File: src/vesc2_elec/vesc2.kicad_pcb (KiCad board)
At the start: 6 copper layers, 0 parts

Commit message: Most the layout done im playing cs2
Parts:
- added C101: 2u2, Capacitor_SMD:C_0603_1608Metric, F.Cu at (150.4, 106.1)
- added C102: 2u2, Capacitor_SMD:C_0603_1608Metric, F.Cu at (150.4, 108.7)
- added C103: 220n, Capacitor_SMD:C_0402_1005Metric, B.Cu at (191.0, 115.5)
- added C104: 220n, Capacitor_SMD:C_0402_1005Metric, B.Cu at (195.5, 116.5)
- added C105: 220n, Capacitor_SMD:C_0402_1005Metric, B.Cu at (198.0, 126.2)
- added C106: 220n, Capacitor_SMD:C_0402_1005Metric, B.Cu at (186.8, 130.5)
- added C107: 220n, Capacitor_SMD:C_0402_1005Metric, B.Cu at (183.0, 119.5)
- added C108: 10p, Capacitor_SMD:C_0402_1005Metric, B.Cu at (181.8, 127.5)
- added C109: 10p, Capacitor_SMD:C_0402_1005Metric, B.Cu at (179.2, 125.2)
- added C110: 4u7, Capacitor_SMD:C_0805_2012Metric, B.Cu at (197.2, 116.8)
- added C111: 10n, Capacitor_SMD:C_0402_1005Metric, F.Cu at (152.0, 115.8)
- added C112: 100n, Capacitor_SMD:C_0402_1005Metric, F.Cu at (152.0, 117.8)
- added C113: 220n, Capacitor_SMD:C_0402_1005Metric, F.Cu at (152.0, 119.8)
- added C114: 33n, Capacitor_SMD:C_0402_1005Metric, B.Cu at (182.3, 121.8)
- added C115: 220n, Capacitor_SMD:C_0402_1005Metric, F.Cu at (152.0, 123.7)
- added C116: 220n, Capacitor_SMD:C_0402_1005Metric, F.Cu at (154.8, 113.9)
- added C117: 220n, Capacitor_SMD:C_0402_1005Metric, F.Cu at (154.8, 115.8)
- added C118: 220n, Capacitor_SMD:C_0402_1005Metric, F.Cu at (154.8, 117.8)
- added C119: 2u2, Capacitor_SMD:C_0603_1608Metric, B.Cu at (194.2, 113.2)
- added C120: 2u2, Capacitor_SMD:C_0603_1608Metric, B.Cu at (192.5, 113.2)
- added C121: 10u, Capacitor_SMD:C_1206_3216Metric, B.Cu at (175.8, 117.8)
- added C122: 2u2, Capacitor_SMD:C_0603_1608Metric, B.Cu at (179.0, 121.0)
- added C123: 10u, Capacitor_SMD:C_1206_3216Metric, B.Cu at (172.0, 120.5)
- added C124: 270u, Capacitor_SMD:CP_Elec_10x10, F.Cu at (193.0, 92.8)
- added C125: 270u, Capacitor_SMD:CP_Elec_10x10, F.Cu at (172.2, 92.5)
- added C201: 1n, Capacitor_SMD:C_0402_1005Metric, B.Cu at (175.0, 115.3)
- added C202: 4u7, Capacitor_SMD:C_1206_3216Metric, B.Cu at (183.8, 113.8)
- added C203: 1n, Capacitor_SMD:C_0402_1005Metric, B.Cu at (172.5, 115.3)
- added C204: 10n, Capacitor_SMD:C_0402_1005Metric, B.Cu at (189.8, 113.1)
- added C205: 2u2, Capacitor_SMD:C_0603_1608Metric, B.Cu at (176.0, 113.3)
- added C206: 2u2, Capacitor_SMD:C_0603_1608Metric, B.Cu at (172.5, 113.3)
- added C207: 100p, Capacitor_SMD:C_0402_1005Metric, B.Cu at (187.8, 114.1)
- added C208: 33n, Capacitor_SMD:C_0603_1608Metric, B.Cu at (179.5, 113.3)
- added C209: 4u7, Capacitor_SMD:C_1210_3225Metric, B.Cu at (171.0, 104.8)
- added C210: 10n, Capacitor_SMD:C_0402_1005Metric, B.Cu at (189.3, 103.3)
- added C211: 100n, Capacitor_SMD:C_0603_1608Metric, B.Cu at (189.3, 100.8)
- added C212: 330n, Capacitor_SMD:C_0603_1608Metric, B.Cu at (183.5, 101.3)
- added C213: 330n, Capacitor_SMD:C_0603_1608Metric, B.Cu at (180.3, 101.3)
- added C214: 330n, Capacitor_SMD:C_0603_1608Metric, B.Cu at (177.0, 101.3)
- added C215: 1n, Capacitor_SMD:C_0402_1005Metric, B.Cu at (174.8, 101.0)
- added C216: 1n, Capacitor_SMD:C_0402_1005Metric, B.Cu at (173.5, 101.0)
- added C217: 4u7, Capacitor_SMD:C_1210_3225Metric, B.Cu at (189.8, 106.8)
- added C218: 22u, Capacitor_SMD:C_1210_3225Metric, B.Cu at (184.0, 97.8)
- added C301: 1n, Capacitor_SMD:C_0402_1005Metric, B.Cu at (194.1, 91.4)
- added C302: 1n, Capacitor_SMD:C_0402_1005Metric, B.Cu at (187.7, 91.5)
- added C303: 3n3, Capacitor_SMD:C_0402_1005Metric, B.Cu at (196.4, 92.0)
- added C401: 1n, Capacitor_SMD:C_0402_1005Metric, B.Cu at (182.4, 91.4)
- added C402: 1n, Capacitor_SMD:C_0402_1005Metric, B.Cu at (176.1, 91.5)
- added C403: 3n3, Capacitor_SMD:C_0402_1005Metric, B.Cu at (184.8, 92.0)
- added C501: 1n, Capacitor_SMD:C_0402_1005Metric, B.Cu at (171.1, 91.4)
- added C502: 1n, Capacitor_SMD:C_0402_1005Metric, B.Cu at (164.7, 91.5)
- added C503: 3n3, Capacitor_SMD:C_0402_1005Metric, B.Cu at (173.4, 92.0)
- added D101: 30V, Diode_SMD:D_SMF, B.Cu at (191.2, 82.5)
- added D102: DTVS, Package_TO_SOT_SMD:SOT-523, F.Cu at (154.7, 129.6)
- added D103: 3V3, Package_DFN_QFN:Diodes_UDFN-10_1.0x2.5mm_P0.5mm, F.Cu at (141.4, 115.0)
- added D104: 3V3, Package_DFN_QFN:Diodes_UDFN-10_1.0x2.5mm_P0.5mm, F.Cu at (144.6, 115.0)
- added D105: WS2812B-2020, Bluesat:WS2812B-2020, F.Cu at (183.0, 130.0)
- added D106: WS2812B-2020, Bluesat:WS2812B-2020, F.Cu at (179.4, 130.0)
- added D107: WS2812B-2020, Bluesat:WS2812B-2020, F.Cu at (175.9, 130.0)
- added D201: D_Schottky, Diode_SMD:D_SOD-123, B.Cu at (187.0, 99.8)
- added J101: XT-30-TOP, Bluesat:XT30PW-M_1x02_P2.50mm_Top_mount, F.Cu at (191.0, 78.5)
- added J102: HALL/ENCODER, Bluesat:SM06B-PASS, F.Cu at (163.0, 108.0)
- added J103: SM02B-PASS, Bluesat:BM02B-PASS, F.Cu at (169.0, 122.0)
- added J104: IDC6, Bluesat:IDC6, F.Cu at (195.0, 106.0)
- added J105: MR_60_TOP, Bluesat:MR60-F-TopMount, F.Cu at (173.0, 80.0)
- added L101: 600R, Resistor_SMD:R_0402_1005Metric, B.Cu at (193.2, 115.5)
- added L201: 47u, Inductor_SMD:L_Changjiang_FXL0630, F.Cu at (184.0, 99.8)
- added Q301: IRFH7440TRPBF, Bluesat:PQFN_5x6mm_E_DGS, B.Cu at (195.2, 87.3)
- added Q302: IRFH7440TRPBF, Bluesat:PQFN_5x6mm_E_DGS, B.Cu at (189.7, 87.3)
- added Q401: IRFH7440TRPBF, Bluesat:PQFN_5x6mm_E_DGS, B.Cu at (183.7, 87.3)
- added Q402: IRFH7440TRPBF, Bluesat:PQFN_5x6mm_E_DGS, B.Cu at (178.1, 87.3)
- added Q501: IRFH7440TRPBF, Bluesat:PQFN_5x6mm_E_DGS, B.Cu at (172.2, 87.3)
- added Q502: IRFH7440TRPBF, Bluesat:PQFN_5x6mm_E_DGS, B.Cu at (166.7, 87.3)
- added R101: 10k, Resistor_SMD:R_0402_1005Metric, F.Cu at (141.1, 107.9)
- added R102: 100k, Resistor_SMD:R_0402_1005Metric, F.Cu at (141.1, 109.9)
- added R103: 2k2, Resistor_SMD:R_0402_1005Metric, F.Cu at (141.1, 111.9)
- added R104: 2k2, Resistor_SMD:R_0402_1005Metric, F.Cu at (144.0, 105.9)
- added R105: 2k2, Resistor_SMD:R_0402_1005Metric, F.Cu at (144.0, 107.9)
- added R106: 10k, Resistor_SMD:R_0402_1005Metric, F.Cu at (144.0, 109.9)
- added R107: 220k, Resistor_SMD:R_0402_1005Metric, B.Cu at (181.2, 119.2)
- added R108: 100k, Resistor_SMD:R_0402_1005Metric, F.Cu at (146.9, 105.9)
- added R109: 10k, Resistor_SMD:R_0402_1005Metric, B.Cu at (181.2, 120.5)
- added R110: 470R, Resistor_SMD:R_0402_1005Metric, B.Cu at (182.2, 123.0)
- added R201: 15k, Resistor_SMD:R_0402_1005Metric, B.Cu at (187.8, 115.3)
- added R202: 4k7, Resistor_SMD:R_0402_1005Metric, B.Cu at (189.3, 110.1)
- added R203: 220k, Resistor_SMD:R_0402_1005Metric, B.Cu at (187.8, 112.8)
- added R204: 1k, Resistor_SMD:R_0402_1005Metric, B.Cu at (180.5, 115.6)
- added R205: 2k2, Resistor_SMD:R_0402_1005Metric, B.Cu at (179.0, 115.6)
- added R206: 1k, Resistor_SMD:R_0402_1005Metric, B.Cu at (176.3, 115.3)
- added R207: 1k, Resistor_SMD:R_0402_1005Metric, B.Cu at (173.8, 115.3)
- added R208: 10k, Resistor_SMD:R_0402_1005Metric, B.Cu at (185.0, 116.1)
- added R209: 10k, Resistor_SMD:R_0402_1005Metric, B.Cu at (182.5, 116.1)
- added R210: 220k, Resistor_SMD:R_0402_1005Metric, B.Cu at (189.3, 111.3)
- added R301: 10R, Resistor_SMD:R_0402_1005Metric, B.Cu at (194.1, 93.8)
- added R302: 10R, Resistor_SMD:R_0402_1005Metric, B.Cu at (187.7, 94.0)
- added R303: 4k7, Resistor_SMD:R_0402_1005Metric, B.Cu at (194.1, 92.5)
- added R304: 4k7, Resistor_SMD:R_0402_1005Metric, B.Cu at (187.7, 92.8)
- added R305: 1m, Resistor_SMD:R_2512_6332Metric, B.Cu at (190.8, 94.8)
- added R306: 10R, Resistor_SMD:R_0402_1005Metric, B.Cu at (197.2, 94.2)
- added R307: 10R, Resistor_SMD:R_0402_1005Metric, B.Cu at (195.8, 94.2)
- added R401: 10R, Resistor_SMD:R_0402_1005Metric, B.Cu at (182.4, 93.8)
- added R402: 10R, Resistor_SMD:R_0402_1005Metric, B.Cu at (176.1, 94.0)
- added R403: 4k7, Resistor_SMD:R_0402_1005Metric, B.Cu at (182.4, 92.5)
- added R404: 4k7, Resistor_SMD:R_0402_1005Metric, B.Cu at (176.1, 92.8)
- added R405: 1m, Resistor_SMD:R_2512_6332Metric, B.Cu at (179.2, 94.8)
- added R406: 10R, Resistor_SMD:R_0402_1005Metric, B.Cu at (185.7, 94.2)
- added R407: 10R, Resistor_SMD:R_0402_1005Metric, B.Cu at (184.2, 94.2)
- added R501: 10R, Resistor_SMD:R_0402_1005Metric, B.Cu at (171.1, 93.8)
- added R502: 10R, Resistor_SMD:R_0402_1005Metric, B.Cu at (164.7, 94.0)
- added R503: 4k7, Resistor_SMD:R_0402_1005Metric, B.Cu at (171.1, 92.5)
- added R504: 4k7, Resistor_SMD:R_0402_1005Metric, B.Cu at (164.7, 92.8)
- added R505: 1m, Resistor_SMD:R_2512_6332Metric, B.Cu at (167.8, 94.8)
- added R506: 10R, Resistor_SMD:R_0402_1005Metric, B.Cu at (174.2, 94.2)
- added R507: 10R, Resistor_SMD:R_0402_1005Metric, B.Cu at (172.8, 94.2)
- added TH101: 10k, Resistor_SMD:R_0402_1005Metric, F.Cu at (146.9, 111.9)
- added U101: STM32G474_VESC, Bluesat:LQFP-64-0.5, B.Cu at (190.5, 123.0)
- added U102: TCAN1462V, Package_SO:SOIC-8_3.9x4.9mm_P1.27mm, B.Cu at (174.5, 125.8)
- added U103: HX4002, Package_TO_SOT_SMD:SOT-23-6, B.Cu at (175.8, 121.0)
- added U201: DRV8301, Bluesat:HTSSOP-56_6.1x14-0.5-EP, B.Cu at (180.5, 107.3)
- added Y101: 24Mhz, Crystal:Crystal_SMD_2016-4Pin_2.0x1.6mm, B.Cu at (181.8, 125.2)
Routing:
- net GND: vias 0 -> 15
- added copper zone on In2.Cu, net GND
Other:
- board outline added: 36 x 57 mm

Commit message: finished routing :)
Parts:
- C101, C102, C111, C112, C113, C115, C116, C117, C118, D102, D103, D104, R101, R102, R103, R104, R105, R106, R108, TH101: moved to B.Cu
- J102: footprint Bluesat:SM06B-PASS -> Bluesat:BM06B-PASS
- moved D103 55.4 mm to (196.8, 113.2), turned to 90 degrees
- moved R102 55.2 mm to (196.2, 107.0)
- moved TH101 54.8 mm to (193.8, 83.4), turned to 180 degrees
- moved R108 46.6 mm to (193.5, 107.0)
- moved R101 40.3 mm to (180.2, 117.5), turned to 180 degrees
- moved C111 39.4 mm to (191.0, 110.5), turned to -90 degrees
- moved C101 34.7 mm to (183.2, 117.2)
- moved C116 34.2 mm to (185.0, 130.0), turned to 180 degrees
- moved C113 31.3 mm to (181.5, 130.0), turned to 180 degrees
- moved R103 27.7 mm to (168.2, 117.2), turned to 180 degrees
- moved C115 26.8 mm to (178.0, 130.0), turned to 180 degrees
- moved C117 25.8 mm to (177.5, 128.2), turned to -90 degrees
- moved R104 25.6 mm to (167.8, 115.5), turned to 180 degrees
- moved R105 22.6 mm to (165.2, 115.5)
- moved R106 21.8 mm to (164.8, 116.8)
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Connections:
- C101 pad 1: GND -> VDD
- C124 pad 1: V_SUPPLY -> VBUS
- C125 pad 1: V_SUPPLY -> VBUS
- C217 pad 1: V_SUPPLY -> VBUS
- D101 pad 1: V_SUPPLY -> VBUS
- D102 pad 1: /CANH -> /CANL
- D102 pad 2: /CANL -> /CANH
- D103 pad 2: /DBG.SWCLK -> /DBG.SWO
- D103 pad 4: /DBG.SWO -> /DBG.SWCLK
- D103 pad 7: /DBG.SWO -> /DBG.SWCLK
- D103 pad 9: /DBG.SWCLK -> /DBG.SWO
- J101 pad 2: V_SUPPLY -> VBUS
- Q301 pad 1: V_SUPPLY -> VBUS
- Q401 pad 1: V_SUPPLY -> VBUS
- Q501 pad 1: V_SUPPLY -> VBUS
- R101 pad 2: GND -> VDD
- R107 pad 1: V_SUPPLY -> VBUS
- TH101 pad 1: VDD -> GND
- U201 pad 53: V_SUPPLY -> VBUS
- U201 pad 54: V_SUPPLY -> VBUS
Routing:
- net VBUS: track 0.00 -> 47.6 mm, vias 0 -> 53
- net /HALL_TEMP: track 0.00 -> 46.4 mm, vias 0 -> 3
- net Net-(U101A-PA3_TMP_BRD): track 0.00 -> 43.3 mm, vias 0 -> 2
- net /HALLW: track 0.00 -> 36.2 mm, vias 0 -> 3
- net /Gate Driver/SDO: track 0.00 -> 35.6 mm, vias 0 -> 2
- net /HALLU: track 0.00 -> 34.0 mm, vias 0 -> 3
- net /HALLV: track 0.00 -> 33.6 mm, vias 0 -> 3
- net /Gate Driver/BR_SO2: track 0.00 -> 31.6 mm, vias 0 -> 2
- net /Gate Driver/SLCK: track 0.00 -> 31.2 mm, vias 0 -> 2
- net /Gate Driver/CS: track 0.00 -> 28.8 mm, vias 0 -> 2
- net /DBG.NRST: track 0.00 -> 28.0 mm, vias 0 -> 3
- net /Gate Driver/SDI: track 0.00 -> 27.6 mm, vias 0 -> 2
- net SNA: track 0.00 -> 26.3 mm, vias 0 -> 2
- net /Gate Driver/BR_SO1: track 0.00 -> 26.0 mm, vias 0 -> 2
- net /Gate Driver/EN_GATE: track 0.00 -> 25.8 mm, vias 0 -> 2
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- added copper zone on B.Cu, net +5V
- added copper zone on B.Cu, net /Gate Driver/H3_LOW
- added copper zone on B.Cu, net /PHASEA
- added copper zone on In3.Cu, net /PHASEA
- added copper zone on B.Cu, net /PHASEB
- added copper zone on In3.Cu, net /PHASEB
- added copper zone on B.Cu, net /PHASEC
- added copper zone on In3.Cu, net /PHASEC
- added copper zone on In1.Cu, net GND
- added copper zone on In4.Cu, net GND
- added copper zone on B.Cu, net Net-(C303-Pad1)
- added copper zone on B.Cu, net Net-(C403-Pad1)
- added copper zone on B.Cu, net Net-(C503-Pad1)
- added copper zone on B.Cu, net Net-(D201-K)
- added copper zone on B.Cu, net Net-(U103-CP+)
- added copper zone on B.Cu, net Net-(U103-CP-)
- added copper zone on B.Cu, net Net-(U201-GVDD)
- added copper zone on B.Cu, net SNA
- added copper zone on B.Cu, net SNB
- added copper zone on B.Cu, net VBUS
- added copper zone on F.Cu, net VBUS
- added copper zone on B.Cu, net VDD
- added copper zone on In2.Cu, net VDD
- added copper zone on B.Cu, net VDDA
- added copper zone on B.Cu, net V_SUPPLY
- removed copper zone on In2.Cu, net GND

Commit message: Fix small global label error
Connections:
- C209 pad 2: V_SUPPLY -> VBUS
- U201 pad 29: V_SUPPLY -> VBUS
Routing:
- net VBUS: vias 53 -> 59
- removed copper zone on B.Cu, net V_SUPPLY

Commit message: HELLO FROM ARCH LINUX (minor changes for QOL when soldering)
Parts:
- moved C203 0.50 mm to (172.5, 115.2)
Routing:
- net /CANH: track 7.11 -> 7.82 mm
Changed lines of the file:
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@@
 	(footprint "Capacitor_SMD:C_0402_1005Metric"
 		(layer "B.Cu")
-		(at 172.54 115.75 -90)
+		(at 172.5 115.25 -90)
 		(descr "Capacitor SMD 0402 (1005 Metric), square (rectangular) end terminal, IPC-7351 nominal, (Body size source: IPC-SM-782 page 76, https://www.pcb-3d.com/wordpress/wp-content/uploads/ipc-sm-782a_amendment_1_and_2.pdf), generated with kicad-footprint-generator")
 		(tags "capacitor")
@@
 	)
 	(via
-		(at 172.54 115.27)
-		(size 0.45)
-		(drill 0.2)
-		(layers "F.Cu" "B.Cu")
-		(net 1)
-	)
-	(via
 		(at 174.5 119.75)
 		(size 0.45)
@@
 	)
 	(via
+		(at 172.5 114.77)
+		(size 0.45)
+		(drill 0.2)
+		(layers "F.Cu" "B.Cu")
+		(net 1)
+	)
+	(via
 		(at 193.75 118.5)
 		(size 0.45)
@@
 	)
 	(segment
-		(start 173.3666 116.23)
-		(end 173.79 115.8066)
+		(start 172.5 115.73)
+		(end 173.7134 115.73)
 		(width 0.2)
 		(layer "B.Cu")
@@
 	)
 	(segment
-		(start 172.54 116.23)
-		(end 173.3666 116.23)
+		(start 173.7134 115.73)
+		(end 173.79 115.8066)
 		(width 0.2)
 		(layer "B.Cu")
@@
 	)
 	(segment
-		(start 169.75 124.5)
-		(end 170 124.75)
-		(width 0.095)
-		(layer "B.Cu")
-		(net 44)
-	)
-	(segment
 		(start 170.525 127.615)
 		(end 170.365 127.615)
@@
 	)
 	(segment
-		(start 167.644999 124.5)
-		(end 169.75 124.5)
+		(start 170 124.25)
+		(end 169.75 124)
 		(width 0.095)
 		(layer "B.Cu")
@@
 	)
 	(segment
-		(start 170 124.75)
-		(end 170 125)
+		(start 170 125)
+		(end 170 124.25)
 		(width 0.095)
 		(layer "B.Cu")
@@
 		(net 44)
 	)
+	(segment
+		(start 169.75 124)
+		(end 168.144999 124)
+		(width 0.095)
+		(layer "B.Cu")
+		(net 44)
+	)
+	(segment
+		(start 168.144999 124)
+		(end 167.644999 124.5)
+		(width 0.095)
+		(layer "B.Cu")
+		(net 44)
+	)
 	(via
 		(at 197 110.77)
@@
 	)
 	(segment
-		(start 188.75 128.675)
-		(end 188.75 127.5)
-		(width 0.095)
+		(start 184.490001 115.75)
+		(end 184.490001 115.240001)
+		(width 0.2)
 		(layer "B.Cu")
 		(net 61)
 	)
 	(segment
-		(start 184.79 112.46)
-		(end 184.79 111.0466)
-		(width 0.2)
+		(start 188.75 128.675)
+		(end 188.75 127.5)
+		(width 0.095)
 		(layer "B.Cu")
 		(net 61)
@@
 	)
 	(segment
-		(start 184.490001 115.240001)
-		(end 184 114.75)
+		(start 185.984 115.234)
+		(end 186.25 115.5)
 		(width 0.2)
 		(layer "B.Cu")
@@
 	)
 	(segment
-		(start 185.984 115.234)
-		(end 186.25 115.5)
+		(start 184.490001 115.240001)
+		(end 184.25 115)
 		(width 0.2)
 		(layer "B.Cu")
@@
 	)
 	(segment
-		(start 184 113.25)
-		(end 184.79 112.46)
+		(start 184.25 115)
+		(end 184.25 113)
 		(width 0.2)
 		(layer "B.Cu")
@@
 	)
 	(segment
-		(start 184.490001 115.75)
-		(end 184.490001 115.240001)
+		(start 184.25 113)
+		(end 184.79 112.46)
 		(width 0.2)
 		(layer "B.Cu")
@@
 	)
 	(segment
-		(start 184 114.75)
-		(end 184 113.25)
+		(start 184.79 112.46)
+		(end 184.79 111.0466)
 		(width 0.2)
 		(layer "B.Cu")

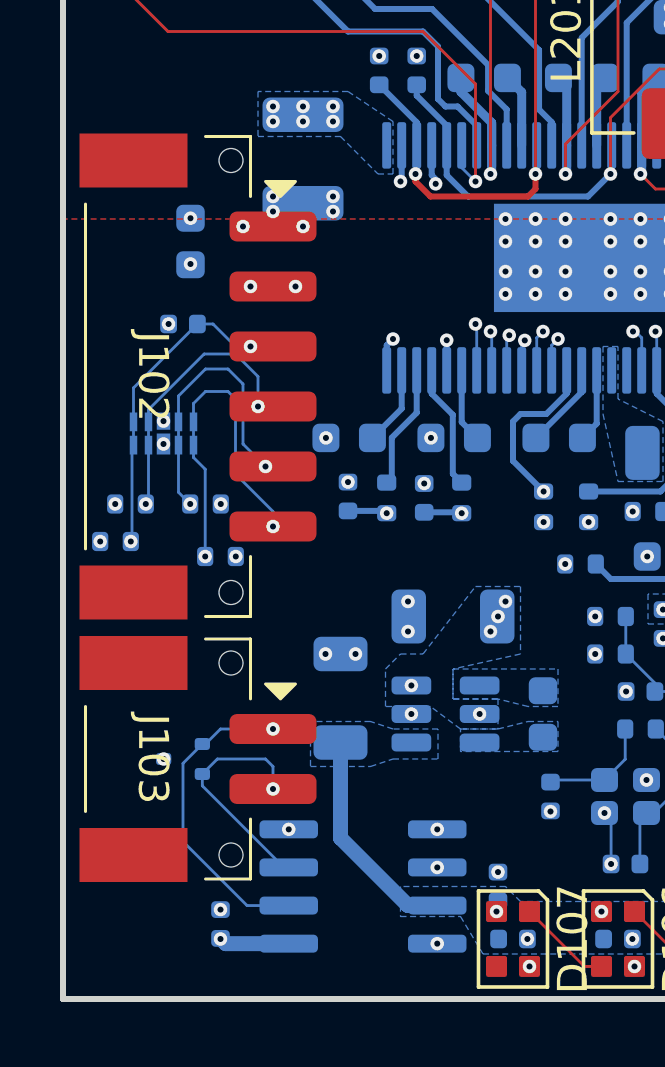
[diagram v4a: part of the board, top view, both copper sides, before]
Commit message: Update footprints of connectors and reroute
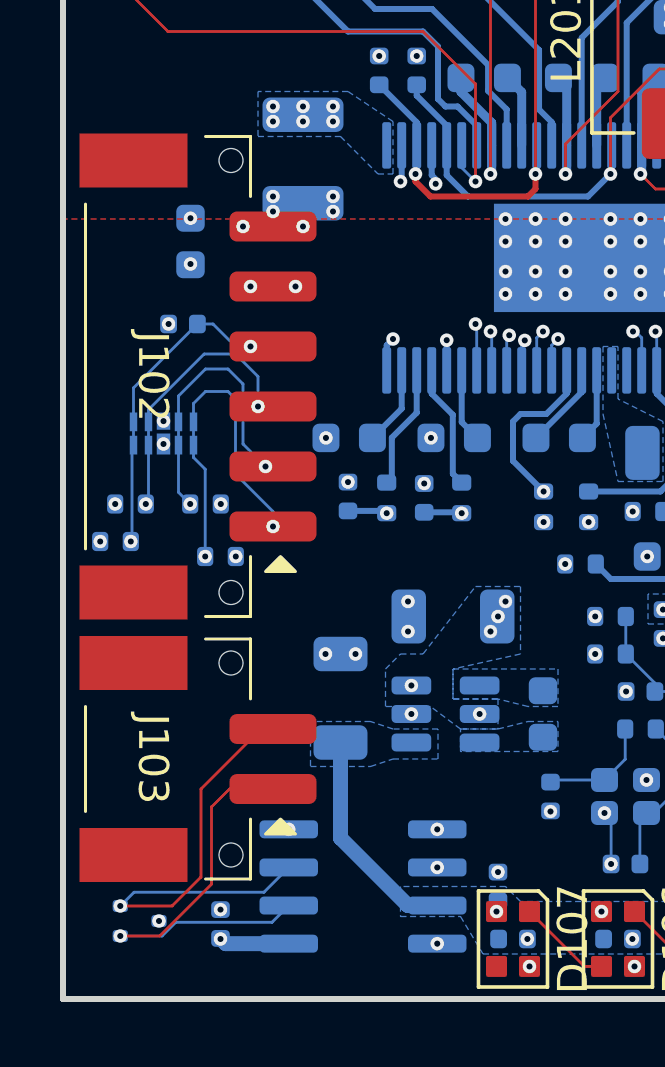
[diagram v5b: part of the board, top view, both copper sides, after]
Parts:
- moved D102 5.59 mm to (165.6, 129.4), turned to 0 degrees
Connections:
- J102 pad 1: GND -> /HALLW
- J102 pad 2: VDD -> /HALLV
- J102 pad 3: /HALL_TEMP -> /HALLU
- J102 pad 4: /HALLU -> /HALL_TEMP
- J102 pad 5: /HALLV -> VDD
- J102 pad 6: /HALLW -> GND
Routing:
- net /CANH: track 7.82 -> 15.4 mm
- net /CANL: track 10.5 -> 14.7 mm
